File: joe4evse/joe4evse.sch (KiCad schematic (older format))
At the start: 37 parts, among them J1 Screw_Terminal_01x03, J2 USB_B_Micro, J3 Screw_Terminal_01x02, J4 Conn_01x06, J5 Screw_Terminal_01x03, J6 Conn_01x09, J8 Conn_01x08, K1 G5LE-1, Q1 AO3402, SW1 SW_DIP_x06, U1 CH340C, U2 MAX3485, U3 TXB0104PW

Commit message: joe/sch: Schematic should be done
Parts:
- removed C4, C5: 100n, Capacitor_SMD:C_0603_1608Metric, symbol Device:C_Small
- removed D3: D_Schottky, Diode_SMD:D_SOD-123, symbol Device:D_Schottky
- removed D4, D5: Green, LED_SMD:LED_0603_1608Metric, symbol Device:LED
- removed J1, J5: Screw_Terminal_01x03, TerminalBlock:TerminalBlock_bornier-3_P5.08mm, symbol Connector:Screw_Terminal_01x03
- removed J3: Screw_Terminal_01x02, TerminalBlock:TerminalBlock_bornier-2_P5.08mm, symbol Connector:Screw_Terminal_01x02
- removed J4: Conn_01x06, Connector_PinHeader_2.54mm:PinHeader_1x06_P2.54mm_Vertical, symbol Connector_Generic:Conn_01x06
- removed J6: Conn_01x09, Connector_PinHeader_2.54mm:PinHeader_1x09_P2.54mm_Vertical, symbol Connector_Generic:Conn_01x09
- removed J8: Conn_01x08, Connector_PinHeader_2.54mm:PinHeader_1x08_P2.54mm_Vertical, symbol Connector_Generic:Conn_01x08
- removed K1: G5LE-1, Relay_THT:Relay_SPDT_Omron-G5LE-1, symbol Relay:G5LE-1
- removed Q1: AO3402, Package_TO_SOT_SMD:SOT-23, symbol ma4evse:AO3402
- removed R11, R12, R5, R7, R8: 100, Resistor_SMD:R_0603_1608Metric, symbol Device:R_Small
- removed R3, R4: 1k, Resistor_SMD:R_0603_1608Metric, symbol Device:R_Small
- removed R6: DNP, Resistor_SMD:R_0603_1608Metric, symbol Device:R_Small
- removed SW1: SW_DIP_x06, Button_Switch_THT:SW_DIP_SPSTx06_Slide_9.78x17.42mm_W7.62mm_P2.54mm, symbol Switch:SW_DIP_x06
- removed U3: TXB0104PW, Package_SO:TSSOP-14_4.4x5mm_P0.65mm, symbol Logic_LevelTranslator:TXB0104PW
- added J1, J3: Conn_01x03, symbol Connector_Generic:Conn_01x03
- added J4, J5: Conn_01x02, symbol Connector_Generic:Conn_01x02
- added J6: CONNFLY_Elec_DS1129-04-S8B0P-X, ma4evse:CONNFLY_Elec_DS1129-04-S8B0P-X, symbol ma4evse:CONNFLY_Elec_DS1129-04-S8B0P-X
- added J7: 8P8C_LED_Shielded, Connector_RJ:RJ45_Amphenol_RJHSE538X, symbol ma4evse:8P8C_LED_Shielded
- added SW1: JS202011CQN, symbol ma4evse:JS202011CQN
- R1, R2: value 10k -> 1k
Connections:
- net labels added: +12V, FIPY_RXD, FIPY_TXD, LED_~CS, MISO, MOSI, NFC_~CS, NFC_~RST, NFC_~RSTO, RELAY_AC, RELAY_JACK, RELAY_RCMB, SCLK, TOUCH
- net labels removed: FIPY_RX, FIPY_TX, FTDI_C_RX, FTDI_C_TX, FTDI_RX, FTDI_TX, GPIO_5_P2, GPIO_5_P21, GPIO_P12, GPIO_P2, GPIO_P21, NFC_CLK, NFC_MISO, NFC_MOSI, NFC_NRST, NFC_NRSTOUT, NFC_SS, RELAY
- wire segments 148 -> 135
- no-connect marks 11 -> 25
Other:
- note added: "RCMB connector\n"
- note added: "The EVSE circuitry"
- note removed: "1 & 2: FiPy - USB\n3 & 4 : ModBUS - USB\n5 & 6 : FiPy - ModBUS"
- note removed: "External 5V UART interface"
- note removed: "FTDI standard pinout.\nMade to be able to plug directly\na FTDI cable."
- note removed: "GPIO Breakout"
- note removed: "NFC Connector"
- note removed: "Power status LEDs"
- note removed: "SPDT relay"
- moved on the sheet: C2, C3, D1, J2, U1

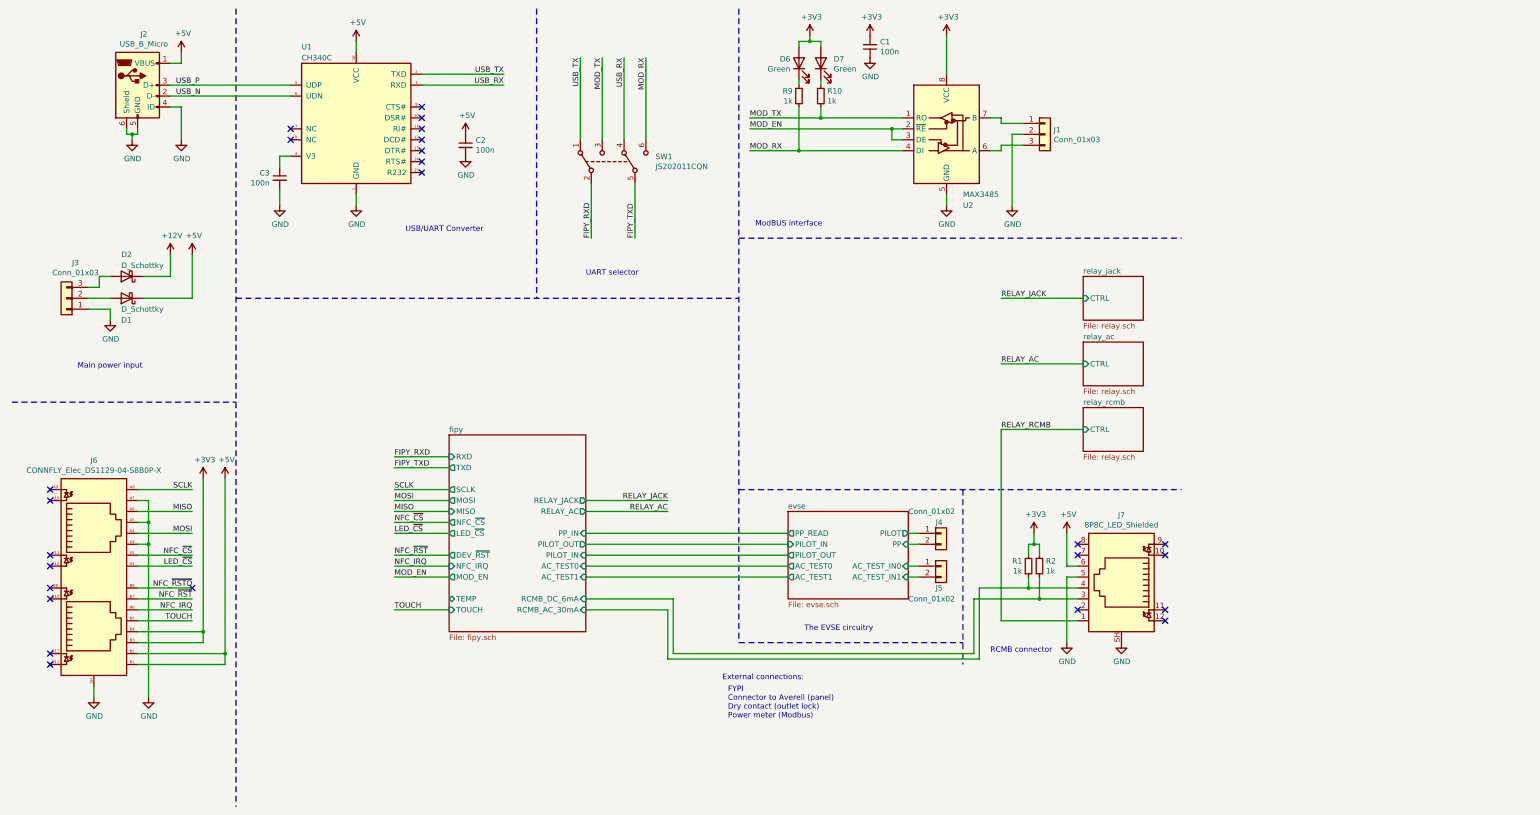
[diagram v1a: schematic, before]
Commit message: joe/sch: Assign footprints to components
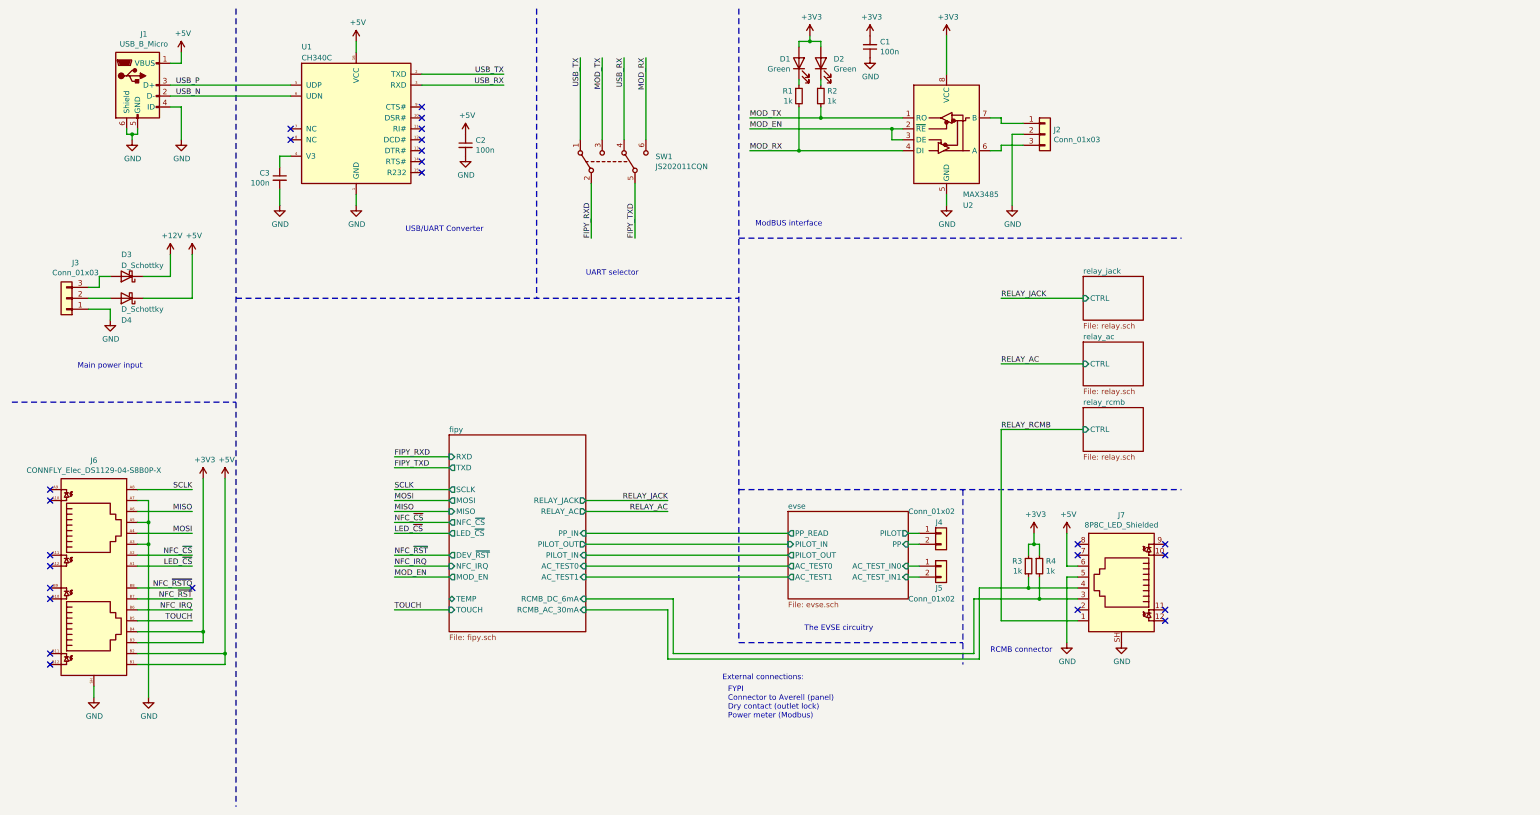
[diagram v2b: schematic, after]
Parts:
- J2: renamed from J1; footprint (none) -> Connector_JST:JST_PH_B3B-PH-K_1x03_P2.00mm_Vertical
- J3: footprint (none) -> Connector_JST:JST_EH_S3B-EH_1x03_P2.50mm_Horizontal
- J4: footprint (none) -> Connector_JST:JST_PH_B2B-PH-K_1x02_P2.00mm_Vertical
- J5: footprint (none) -> Connector_JST:JST_NV_B02P-NV_1x02_P5.00mm_Vertical
- SW1: footprint (none) -> ma4evse:JS202011CQN
- renumbered D6 to D1, D7 to D2, D2 to D3, D1 to D4, J2 to J1, R9 to R1, R10 to R2, R1 to R3, R2 to R4
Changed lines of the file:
@@
 $EndComp
 $Comp
-L Connector:USB_B_Micro J2
+L Connector:USB_B_Micro J1
 U 1 1 5D2617CC
 P 1650 1200
-F 0 "J2" H 1707 1667 50  0000 C CNN
+F 0 "J1" H 1707 1667 50  0000 C CNN
 F 1 "USB_B_Micro" H 1707 1576 50  0000 C CNN
 F 2 "Connector_USB:USB_Micro-B_Molex_47346-0001" H 1800 1150 50  0001 C CNN
@@
 $EndComp
 $Comp
-L power:+5V #PWR0101
+L power:+5V #PWR05
 U 1 1 5D2733A6
 P 2050 900
-F 0 "#PWR0101" H 2050 750 50  0001 C CNN
+F 0 "#PWR05" H 2050 750 50  0001 C CNN
 F 1 "+5V" H 2065 1073 50  0000 C CNN
 F 2 "" H 2050 900 50  0001 C CNN
@@
 $EndComp
 $Comp
-L power:GND #PWR0102
+L power:GND #PWR08
 U 1 1 5D274239
 P 1600 1700
-F 0 "#PWR0102" H 1600 1450 50  0001 C CNN
+F 0 "#PWR08" H 1600 1450 50  0001 C CNN
 F 1 "GND" H 1605 1527 50  0000 C CNN
 F 2 "" H 1600 1700 50  0001 C CNN
@@
 	2050 1000 2050 900
 $Comp
-L power:GND #PWR0103
+L power:GND #PWR09
 U 1 1 5D277783
 P 2050 1700
-F 0 "#PWR0103" H 2050 1450 50  0001 C CNN
+F 0 "#PWR09" H 2050 1450 50  0001 C CNN
 F 1 "GND" H 2055 1527 50  0000 C CNN
 F 2 "" H 2050 1700 50  0001 C CNN
@@
 	2050 1400 2050 1700
 $Comp
-L power:+5V #PWR0104
+L power:+5V #PWR016
 U 1 1 5D27C44A
 P 2150 2750
-F 0 "#PWR0104" H 2150 2600 50  0001 C CNN
+F 0 "#PWR016" H 2150 2600 50  0001 C CNN
 F 1 "+5V" H 2165 2923 50  0000 C CNN
 F 2 "" H 2150 2750 50  0001 C CNN
@@
 	2150 3150 2150 2750
 $Comp
-L power:GND #PWR0105
+L power:GND #PWR017
 U 1 1 5D27C4DB
 P 1400 3350
-F 0 "#PWR0105" H 1400 3100 50  0001 C CNN
+F 0 "#PWR017" H 1400 3100 50  0001 C CNN
 F 1 "GND" H 1405 3177 50  0000 C CNN
 F 2 "" H 1400 3350 50  0001 C CNN
@@
 Main power input
 $Comp
-L power:GND #PWR0118
+L power:GND #PWR014
 U 1 1 5D2C078F
 P 9650 2300
-F 0 "#PWR0118" H 9650 2050 50  0001 C CNN
+F 0 "#PWR014" H 9650 2050 50  0001 C CNN
 F 1 "GND" H 9655 2127 50  0000 C CNN
 F 2 "" H 9650 2300 50  0001 C CNN
@@
 	9650 1650 9750 1650
 $Comp
-L power:+3V3 #PWR0119
+L power:+3V3 #PWR03
 U 1 1 5D2D0961
 P 9050 750
-F 0 "#PWR0119" H 9050 600 50  0001 C CNN
+F 0 "#PWR03" H 9050 600 50  0001 C CNN
 F 1 "+3V3" H 9065 923 50  0000 C CNN
 F 2 "" H 9050 750 50  0001 C CNN
@@
 $EndComp
 $Comp
-L power:GND #PWR0120
+L power:GND #PWR013
 U 1 1 5D2D0F7A
 P 9050 2300
-F 0 "#PWR0120" H 9050 2050 50  0001 C CNN
+F 0 "#PWR013" H 9050 2050 50  0001 C CNN
 F 1 "GND" H 9055 2127 50  0000 C CNN
 F 2 "" H 9050 2300 50  0001 C CNN
@@
 	9050 750  9050 1100
 $Comp
-L power:+3V3 #PWR0121
+L power:+3V3 #PWR02
 U 1 1 5D2D6443
 P 8350 750
-F 0 "#PWR0121" H 8350 600 50  0001 C CNN
+F 0 "#PWR02" H 8350 600 50  0001 C CNN
 F 1 "+3V3" H 8365 923 50  0000 C CNN
 F 2 "" H 8350 750 50  0001 C CNN
@@
 $EndComp
 $Comp
-L power:GND #PWR0122
+L power:GND #PWR06
 U 1 1 5D2D69AC
 P 8350 950
-F 0 "#PWR0122" H 8350 700 50  0001 C CNN
+F 0 "#PWR06" H 8350 700 50  0001 C CNN
 F 1 "GND" H 8355 777 50  0000 C CNN
 F 2 "" H 8350 950 50  0001 C CNN
@@
 NoConn ~ 3050 1700
 $Comp
-L power:GND #PWR0129
+L power:GND #PWR012
 U 1 1 5D398BBB
 P 3650 2300
-F 0 "#PWR0129" H 3650 2050 50  0001 C CNN
+F 0 "#PWR012" H 3650 2050 50  0001 C CNN
 F 1 "GND" H 3655 2127 50  0000 C CNN
 F 2 "" H 3650 2300 50  0001 C CNN
@@
 $EndComp
 $Comp
-L power:+5V #PWR0130
+L power:+5V #PWR04
 U 1 1 5D3992AF
 P 3650 800
-F 0 "#PWR0130" H 3650 650 50  0001 C CNN
+F 0 "#PWR04" H 3650 650 50  0001 C CNN
 F 1 "+5V" H 3665 973 50  0000 C CNN
 F 2 "" H 3650 800 50  0001 C CNN
@@
 	3650 800  3650 900
 $Comp
-L power:GND #PWR0131
+L power:GND #PWR011
 U 1 1 5D3B31ED
 P 2950 2300
-F 0 "#PWR0131" H 2950 2050 50  0001 C CNN
+F 0 "#PWR011" H 2950 2050 50  0001 C CNN
 F 1 "GND" H 2955 2127 50  0000 C CNN
 F 2 "" H 2950 2300 50  0001 C CNN
@@
 $EndComp
 $Comp
-L power:+5V #PWR0132
+L power:+5V #PWR07
 U 1 1 5D41F060
 P 4650 1650
-F 0 "#PWR0132" H 4650 1500 50  0001 C CNN
+F 0 "#PWR07" H 4650 1500 50  0001 C CNN
 F 1 "+5V" H 4665 1823 50  0000 C CNN
 F 2 "" H 4650 1650 50  0001 C CNN
@@
 $EndComp
 $Comp
-L power:GND #PWR0133
+L power:GND #PWR010
 U 1 1 5D41F066
 P 4650 1850
-F 0 "#PWR0133" H 4650 1600 50  0001 C CNN
+F 0 "#PWR010" H 4650 1600 50  0001 C CNN
 F 1 "GND" H 4655 1677 50  0000 C CNN
 F 2 "" H 4650 1850 50  0001 C CNN
@@
 $EndComp
 $Comp
-L Device:D_Schottky D1
+L Device:D_Schottky D4
 U 1 1 5D4319B1
 P 1550 3150
-F 0 "D1" H 1600 3350 50  0000 R CNN
+F 0 "D4" H 1600 3350 50  0000 R CNN
 F 1 "D_Schottky" H 1600 3250 50  0000 R CNN
 F 2 "Diode_SMD:D_SOD-123" H 1550 3150 50  0001 C CNN
@@
 MOD_RX
 $Comp
-L Device:LED D7
+L Device:LED D2
 U 1 1 5D772F44
 P 7900 1000
-F 0 "D7" V 7939 883 50  0000 R CNN
+F 0 "D2" V 7939 883 50  0000 R CNN
 F 1 "Green" V 7848 883 50  0000 R CNN
 F 2 "LED_SMD:LED_0603_1608Metric" H 7900 1000 50  0001 C CNN
@@
 $EndComp
 $Comp
-L Device:R_Small R10
+L Device:R_Small R2
 U 1 1 5D772F50
 P 7900 1300
-F 0 "R10" H 7959 1346 50  0000 L CNN
+F 0 "R2" H 7959 1346 50  0000 L CNN
 F 1 "1k" H 7959 1255 50  0000 L CNN
 F 2 "Resistor_SMD:R_0603_1608Metric" H 7900 1300 50  0001 C CNN
@@
 	7700 1150 7700 1200
 $Comp
-L Device:R_Small R9
+L Device:R_Small R1
 U 1 1 5D795D7B
 P 7700 1300
-F 0 "R9" H 7642 1346 50  0000 R CNN
+F 0 "R1" H 7642 1346 50  0000 R CNN
 F 1 "1k" H 7642 1255 50  0000 R CNN
 F 2 "Resistor_SMD:R_0603_1608Metric" H 7700 1300 50  0001 C CNN
@@
 $EndComp
 $Comp
-L Device:LED D6
+L Device:LED D1
 U 1 1 5D795D6F
 P 7700 1000
-F 0 "D6" V 7739 1079 50  0000 L CNN
+F 0 "D1" V 7739 1079 50  0000 L CNN
 F 1 "Green" V 7648 1079 50  0000 L CNN
 F 2 "LED_SMD:LED_0603_1608Metric" H 7700 1000 50  0001 C CNN
@@
 F 0 "J3" H 918 2825 50  0000 C CNN
 F 1 "Conn_01x03" H 918 2916 50  0000 C CNN
-F 2 "" H 1000 3150 50  0001 C CNN
+F 2 "Connector_JST:JST_EH_S3B-EH_1x03_P2.50mm_Horizontal" H 1000 3150 50  0001 C CNN
 F 3 "~" H 1000 3150 50  0001 C CNN
 	1    1000 3150
@@
 $EndComp
 $Comp
-L Device:D_Schottky D2
+L Device:D_Schottky D3
 U 1 1 5E2741F8
 P 1550 2950
-F 0 "D2" H 1600 2750 50  0000 R CNN
+F 0 "D3" H 1600 2750 50  0000 R CNN
 F 1 "D_Schottky" H 1600 2850 50  0000 R CNN
 F 2 "Diode_SMD:D_SOD-123" H 1550 2950 50  0001 C CNN
@@
 	1950 2950 1950 2750
 $Comp
-L power:+12V #PWR02
+L power:+12V #PWR015
 U 1 1 5E28A95B
 P 1950 2750
-F 0 "#PWR02" H 1950 2600 50  0001 C CNN
+F 0 "#PWR015" H 1950 2600 50  0001 C CNN
 F 1 "+12V" H 1965 2923 50  0000 C CNN
 F 2 "" H 1950 2750 50  0001 C CNN
@@
 $EndComp
 $Comp
-L Connector_Generic:Conn_01x03 J1
+L Connector_Generic:Conn_01x03 J2
 U 1 1 5E290D0B
 P 9950 1650
-F 0 "J1" H 10030 1692 50  0000 L CNN
+F 0 "J2" H 10030 1692 50  0000 L CNN
 F 1 "Conn_01x03" H 10030 1601 50  0000 L CNN
-F 2 "" H 9950 1650 50  0001 C CNN
+F 2 "Connector_JST:JST_PH_B3B-PH-K_1x03_P2.00mm_Vertical" H 9950 1650 50  0001 C CNN
 F 3 "~" H 9950 1650 50  0001 C CNN
 	1    9950 1650
@@
 F 0 "J5" H 8950 5400 50  0000 L CNN
 F 1 "Conn_01x02" H 8700 5300 50  0000 L CNN
-F 2 "" H 9000 5600 50  0001 C CNN
+F 2 "Connector_JST:JST_NV_B02P-NV_1x02_P5.00mm_Vertical" H 9000 5600 50  0001 C CNN
 F 3 "~" H 9000 5600 50  0001 C CNN
 	1    9000 5600
@@
 F 0 "J4" H 8950 5400 50  0000 L CNN
 F 1 "Conn_01x02" H 8700 5500 50  0000 L CNN
-F 2 "" H 9000 5300 50  0001 C CNN
+F 2 "Connector_JST:JST_PH_B2B-PH-K_1x02_P2.00mm_Vertical" H 9000 5300 50  0001 C CNN
 F 3 "~" H 9000 5300 50  0001 C CNN
 	1    9000 5300
@@
 NoConn ~ 11050 6100
 $Comp
-L power:GND #PWR08
+L power:GND #PWR023
 U 1 1 5E03F7E7
 P 10650 6300
-F 0 "#PWR08" H 10650 6050 50  0001 C CNN
+F 0 "#PWR023" H 10650 6050 50  0001 C CNN
 F 1 "GND" H 10655 6127 50  0000 C CNN
 F 2 "" H 10650 6300 50  0001 C CNN
@@
 $EndComp
 $Comp
-L power:GND #PWR07
+L power:GND #PWR022
 U 1 1 5E040938
 P 10150 6300
-F 0 "#PWR07" H 10150 6050 50  0001 C CNN
+F 0 "#PWR022" H 10150 6050 50  0001 C CNN
 F 1 "GND" H 10155 6127 50  0000 C CNN
 F 2 "" H 10150 6300 50  0001 C CNN
@@
 $EndComp
 $Comp
-L power:+5V #PWR06
+L power:+5V #PWR021
 U 1 1 5E0418AA
 P 10150 5300
-F 0 "#PWR06" H 10150 5150 50  0001 C CNN
+F 0 "#PWR021" H 10150 5150 50  0001 C CNN
 F 1 "+5V" H 10165 5473 50  0000 C CNN
 F 2 "" H 10150 5300 50  0001 C CNN
@@
 	9550 6100 10250 6100
 $Comp
-L Device:R_Small R2
+L Device:R_Small R4
 U 1 1 5E06420A
 P 9900 5600
-F 0 "R2" H 9959 5646 50  0000 L CNN
+F 0 "R4" H 9959 5646 50  0000 L CNN
 F 1 "1k" H 9959 5555 50  0000 L CNN
 F 2 "Resistor_SMD:R_0603_1608Metric" H 9900 5600 50  0001 C CNN
@@
 $EndComp
 $Comp
-L Device:R_Small R1
+L Device:R_Small R3
 U 1 1 5E065322
 P 9800 5600
-F 0 "R1" H 9742 5554 50  0000 R CNN
+F 0 "R3" H 9742 5554 50  0000 R CNN
 F 1 "1k" H 9742 5645 50  0000 R CNN
 F 2 "Resistor_SMD:R_0603_1608Metric" H 9800 5600 50  0001 C CNN
@@
 	9900 5900 9300 5900
 $Comp
-L power:+3V3 #PWR05
+L power:+3V3 #PWR020
 U 1 1 5E06DB0D
 P 9850 5300
-F 0 "#PWR05" H 9850 5150 50  0001 C CNN
+F 0 "#PWR020" H 9850 5150 50  0001 C CNN
 F 1 "+3V3" H 9865 5473 50  0000 C CNN
 F 2 "" H 9850 5300 50  0001 C CNN
@@
 NoConn ~ 850  6500
 $Comp
-L power:GND #PWR09
+L power:GND #PWR024
 U 1 1 5E0F6C0A
 P 1250 6800
-F 0 "#PWR09" H 1250 6550 50  0001 C CNN
+F 0 "#PWR024" H 1250 6550 50  0001 C CNN
 F 1 "GND" H 1255 6627 50  0000 C CNN
 F 2 "" H 1250 6800 50  0001 C CNN
@@
 $EndComp
 $Comp
-L power:GND #PWR010
+L power:GND #PWR025
 U 1 1 5E0F7770
 P 1750 6800
-F 0 "#PWR010" H 1750 6550 50  0001 C CNN
+F 0 "#PWR025" H 1750 6550 50  0001 C CNN
 F 1 "GND" H 1755 6627 50  0000 C CNN
 F 2 "" H 1750 6800 50  0001 C CNN
@@
 FIPY_TXD
 $Comp
-L power:+5V #PWR04
+L power:+5V #PWR019
 U 1 1 5E1B6D11
 P 2450 4800
-F 0 "#PWR04" H 2450 4650 50  0001 C CNN
+F 0 "#PWR019" H 2450 4650 50  0001 C CNN
 F 1 "+5V" H 2465 4973 50  0000 C CNN
 F 2 "" H 2450 4800 50  0001 C CNN
@@
 $EndComp
 $Comp
-L power:+3V3 #PWR03
+L power:+3V3 #PWR018
 U 1 1 5E1BE4E5
 P 2250 4800
-F 0 "#PWR03" H 2250 4650 50  0001 C CNN
+F 0 "#PWR018" H 2250 4650 50  0001 C CNN
 F 1 "+3V3" H 2265 4973 50  0000 C CNN
 F 2 "" H 2250 4800 50  0001 C CNN
@@
 F 0 "SW1" V 6046 1512 50  0000 R CNN
 F 1 "JS202011CQN" V 5955 1512 50  0000 R CNN
-F 2 "" H 6000 2100 50  0001 C CNN
+F 2 "ma4evse:JS202011CQN" H 6000 2100 50  0001 C CNN
 F 3 "~" H 6000 2100 50  0001 C CNN
 	1    6000 1900
